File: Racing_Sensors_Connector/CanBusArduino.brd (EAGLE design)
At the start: 160 x 100 mm, 15 parts, among them Y1 16MHz

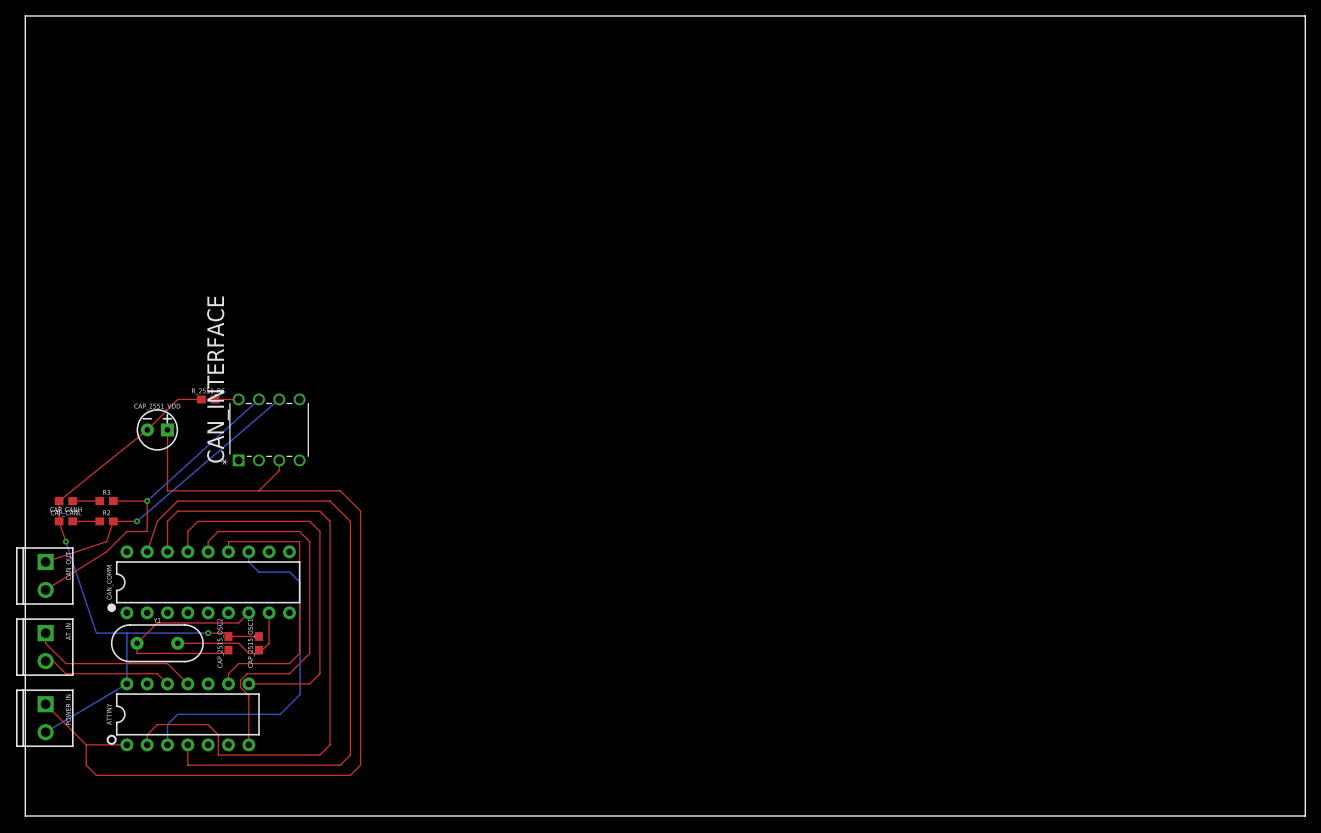
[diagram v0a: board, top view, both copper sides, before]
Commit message: Add CAN communiator for ATmega328P
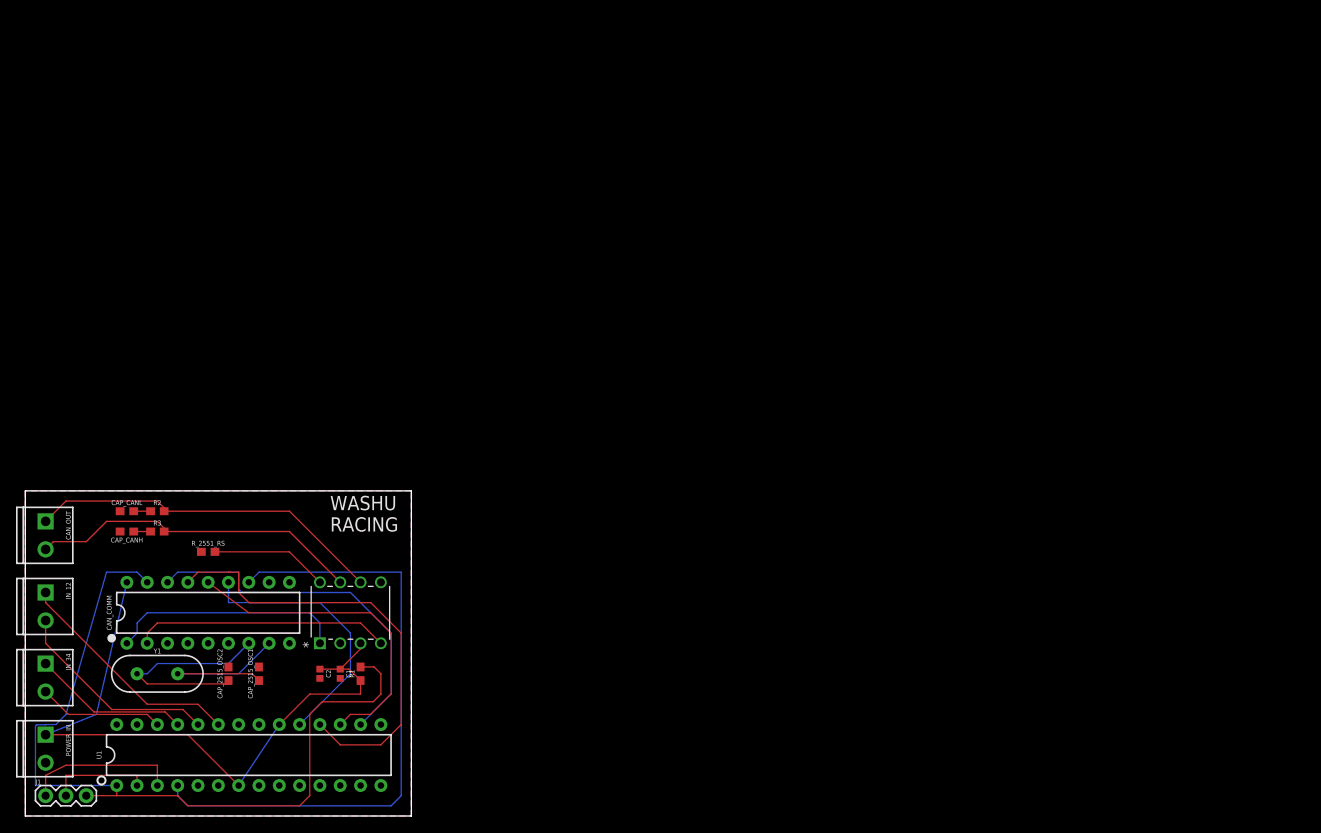
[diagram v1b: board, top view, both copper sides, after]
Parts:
- removed ATTINY: ATTINY84ATTINY84-20PU, SparkFun-IC-Microcontroller:DIP14
- removed AT_IN: (no value), SparkFun-Connectors:SCREWTERMINAL-3.5MM-2
- removed CAP_2551_VDD: 10uF, SparkFun-Capacitors:CPOL-RADIAL-2.5MM-5MM
- added C1, C2: 0.1uF, SparkFun-Capacitors:0402
- added IN_12, IN_34: (no value), SparkFun-Connectors:SCREWTERMINAL-3.5MM-2
- added J1: 455-1750-1-ND, SparkFun-Connectors:1X03
- added R1: 10k, SparkFun-Resistors:0603
- added U1: 328P, SparkFun-IC-Microcontroller:DIP28
- CAN_INTERFACE: value MCP2551-E/P -> MCP2551-I/P; device mcp2551dip:DIP254P762X432-8 -> can_transceiver:DIP254P762X432-8
- moved CAN_INTERFACE 25.0 mm to (44.5, 29.2)
- moved R_2551_RS 19.0 mm to (22.9, 33.0)
- moved CAP_CANH 8.52 mm to (12.7, 35.6)
- moved CAP_CANL 7.73 mm to (12.7, 38.1)
- moved R3 7.41 mm to (16.5, 35.6)
- moved R2 6.48 mm to (16.5, 38.1)
- moved CAN_OUT 5.08 mm to (2.54, 36.8)
- moved CAN_COMM 3.81 mm to (22.9, 25.4)
- moved POWER_IN 3.81 mm to (2.54, 10.2)
- moved CAP_2515_OSC1 3.81 mm to (29.2, 17.8)
- moved CAP_2515_OSC2 3.81 mm to (25.4, 17.8)
- moved Y1 3.81 mm to (16.5, 17.8)
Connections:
- net N$2 renamed CI_RS
- net N$3 renamed CANL
- net N$4 renamed CANH
- removed net VDD: CAN_COMM.18
- removed net VSS: CAN_COMM.9
- removed net XB_RX: ATTINY.12, AT_IN.2
- removed net XB_TX: ATTINY.11, AT_IN.1
- new net IN1: IN_12.1, U1.23
- new net IN2: IN_12.2, U1.24
- new net IN3: IN_34.1, U1.25
- new net IN4: IN_34.2, U1.26
- new net RX: J1.2, U1.2
- new net TX: J1.1, U1.3
- net CAN_CS: now also U1.16; no longer ATTINY.2
- net CAN_INT: now also U1.4; no longer ATTINY.3
- net CAN_RXD: now also CAN_INTERFACE.4
- net CAN_TXD: now also CAN_INTERFACE.1
- net GND: now also C1.2, C2.2, CAN_COMM.9, CAN_INTERFACE.2, U1.22, U1.8; no longer ATTINY.14, CAP_2551_VDD.2
- net MISO: now also U1.18; no longer ATTINY.8
- net MOSI: now also U1.17; no longer ATTINY.7
- net RS: now also J1.3, R1.2, U1.1; no longer ATTINY.4
- net SCK: now also U1.19; no longer ATTINY.9
- net VCC: now also C1.1, C2.1, CAN_COMM.18, R1.1, U1.20, U1.7; no longer ATTINY.1, CAP_2551_VDD.1
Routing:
- net GND: track 78.4 -> 0.00 mm, vias 2 -> 0
- net VCC: track 119.6 -> 83.1 mm
- net CAN_CS: track 81.4 -> 45.9 mm
- net CAN_INT: track 43.4 -> 77.8 mm
- net CAN_RXD: track 0.00 -> 32.1 mm
- net CAN_TXD: track 0.00 -> 29.5 mm
- net IN1: track 0.00 -> 29.2 mm
- net IN2: track 0.00 -> 26.1 mm
- net XB_TX: track 21.2 -> 0.00 mm
- net IN3: track 0.00 -> 19.7 mm
- net TX: track 0.00 -> 19.3 mm
- net RS: track 82.8 -> 101.9 mm
- net XB_RX: track 16.4 -> 0.00 mm
- net IN4: track 0.00 -> 15.7 mm
- net RX: track 0.00 -> 12.7 mm
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- added copper zone on layer 1, net GND
- added copper zone on layer 16, net GND
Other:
- board size 160 x 100 mm -> 48.3 x 40.6 mm
- board text added: "WASHU RACING"
- board text added: "WASHU RACING 2017-18"

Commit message: Update drawing
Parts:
- removed CAN_OUT, IN_12, IN_34, POWER_IN: (no value), SparkFun-Connectors:SCREWTERMINAL-3.5MM-2
- added ADC0/1, ADC2/3, ADC4/5, CANH/L, DIO, PWR: (no value), SparkFun-Connectors:MOLEX-1X2
- renumbered J1 to PRGM
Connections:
- net N$1 renamed OSC1
- net N$5 renamed OSC2
- removed net IN1: IN_12.1, U1.23
- removed net IN2: IN_12.2, U1.24
- removed net IN3: IN_34.1, U1.25
- removed net IN4: IN_34.2, U1.26
- new net A0: ADC0/1.1, U1.23
- new net A1: ADC0/1.2, U1.24
- new net A2: ADC2/3.1, U1.25
- new net A3: ADC2/3.2, U1.26
- new net A4: ADC4/5.1, U1.27
- new net A5: ADC4/5.2, U1.28
- new net D3: DIO.2, U1.5
- new net D4: DIO.1, U1.6
- net CANH: now also CANH/L.2; no longer CAN_OUT.2
- net CANL: now also CANH/L.1; no longer CAN_OUT.1
- net GND: now also PWR.2; no longer POWER_IN.2
- net VCC: now also PWR.1; no longer POWER_IN.1
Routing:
- net A0: track 0.00 -> 30.4 mm
- net IN1: track 29.2 -> 0.00 mm
- net IN2: track 26.1 -> 0.00 mm
- net A1: track 0.00 -> 26.1 mm
- net D4: track 0.00 -> 25.8 mm
- net D3: track 0.00 -> 22.2 mm
- net A2: track 0.00 -> 21.8 mm
- net IN3: track 19.7 -> 0.00 mm
- net A3: track 0.00 -> 18.2 mm
- net IN4: track 15.7 -> 0.00 mm
- net A4: track 0.00 -> 14.6 mm
- net A5: track 0.00 -> 11.0 mm
- net RS: track 101.9 -> 105.9 mm
- net VCC: track 83.1 -> 79.5 mm
- net RX: track 12.7 -> 11.2 mm
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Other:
- outline, holes or cut-outs redrawn
- board text removed: "WASHU RACING"
